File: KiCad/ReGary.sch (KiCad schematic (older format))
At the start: 10 parts, among them U4 SN74CBT16210, U5 SN74CBT16210, U6 SN74CBT16210, U7 SN74CBT16210, U8 PLCC_84_plug, U9 PLCC_84_plug

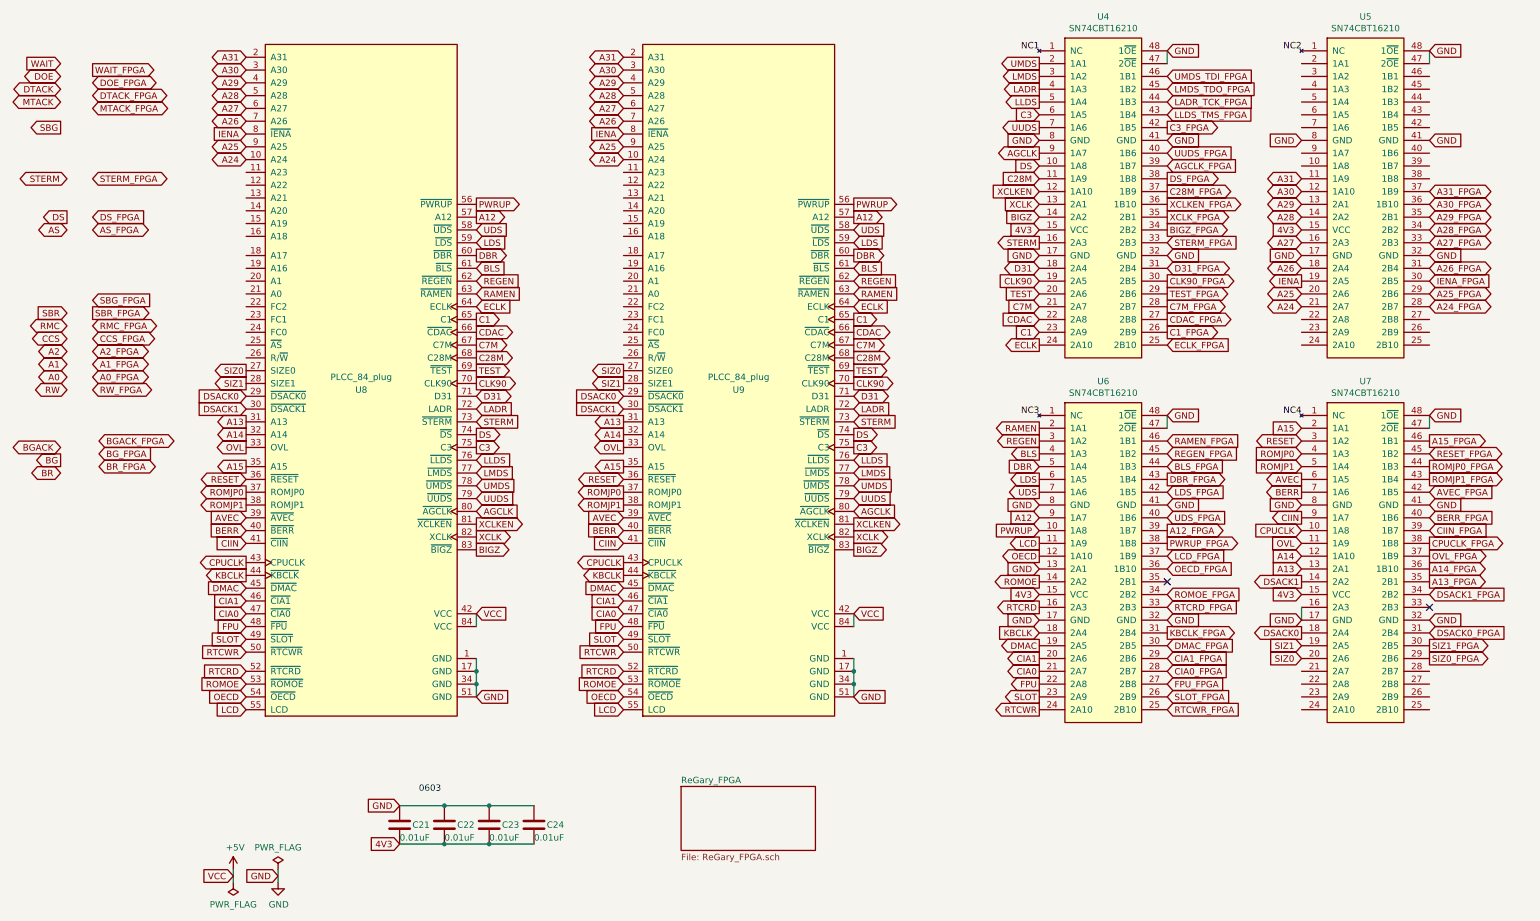
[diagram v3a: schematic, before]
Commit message: More pin assignments and routing
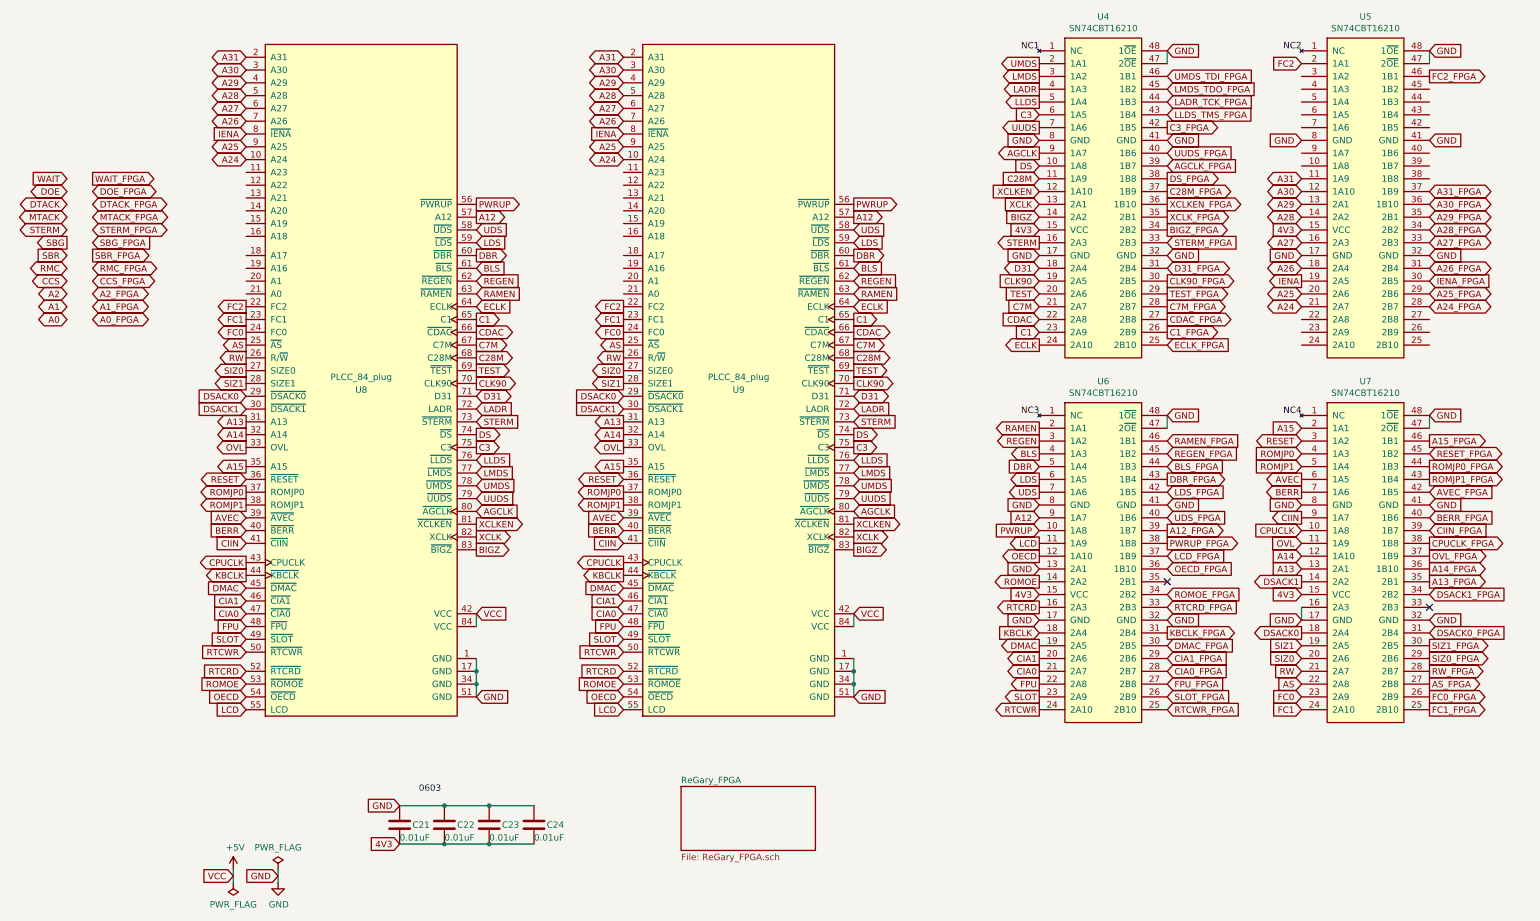
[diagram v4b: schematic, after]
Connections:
- net AS: now also U7.22 (2A8), U8.25 (~AS), U9.25 (~AS)
- net AS_FPGA: now also U7.27 (2B8)
- net RW: now also U7.21 (2A7), U8.26 (R/~W), U9.26 (R/~W)
- net RW_FPGA: now also U7.28 (2B7)
- net FC2: now reaches U5.2 (1A1)
- net FC2: now also U8.22 (FC2), U9.22 (FC2)
- net FC2_FPGA: now reaches U5.46 (1B1)
- net FC0: now reaches U7.23 (2A9)
- net FC0: now also U8.24 (FC0), U9.24 (FC0)
- net FC1: now reaches U7.24 (2A10)
- net FC1: now also U8.23 (FC1), U9.23 (FC1)
- net FC1_FPGA: now reaches U7.25 (2B10)
- net FC0_FPGA: now reaches U7.26 (2B9)
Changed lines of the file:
@@
 Text GLabel 8150 1950 2    50   Output ~ 0
 DS_FPGA
-Text GLabel -250 1100 2    50   Output ~ 0
+Text GLabel -250 1950 2    50   Output ~ 0
 WAIT_FPGA
-Text GLabel -250 1200 2    50   BiDi ~ 0
+Text GLabel -250 2050 2    50   BiDi ~ 0
 DOE_FPGA
-Text GLabel -250 1300 2    50   BiDi ~ 0
+Text GLabel -250 2150 2    50   BiDi ~ 0
 DTACK_FPGA
-Text GLabel -250 1400 2    50   BiDi ~ 0
+Text GLabel -250 2250 2    50   BiDi ~ 0
 MTACK_FPGA
-Text GLabel -250 3000 2    50   Output ~ 0
+Text GLabel -250 2550 2    50   Output ~ 0
 SBR_FPGA
-Text GLabel -250 3100 2    50   BiDi ~ 0
+Text GLabel -250 2650 2    50   BiDi ~ 0
 RMC_FPGA
-Text GLabel -250 3200 2    50   BiDi ~ 0
+Text GLabel -250 2750 2    50   BiDi ~ 0
 CCS_FPGA
-Text GLabel -250 3300 2    50   BiDi ~ 0
+Text GLabel -250 2850 2    50   BiDi ~ 0
 A2_FPGA
-Text GLabel -250 3400 2    50   BiDi ~ 0
+Text GLabel -250 2950 2    50   BiDi ~ 0
 A1_FPGA
-Text GLabel -250 2900 2    50   Input ~ 0
+Text GLabel -250 2450 2    50   Input ~ 0
 SBG_FPGA
-Text GLabel -250 3600 2    50   BiDi ~ 0
+Text GLabel 10200 5800 2    50   Output ~ 0
 RW_FPGA
 Text GLabel 10200 5700 2    50   Output ~ 0
 SIZ0_FPGA
-Text GLabel -250 1950 2    50   BiDi ~ 0
+Text GLabel -250 2350 2    50   BiDi ~ 0
 STERM_FPGA
-Text GLabel -250 2250 2    50   Input ~ 0
-DS_FPGA
-Text GLabel -250 2350 2    50   BiDi ~ 0
+Text GLabel 10200 5900 2    50   Output ~ 0
 AS_FPGA
 Text GLabel 8150 4000 2    50   Input ~ 0
@@
 Text GLabel 10200 4800 2    50   Output ~ 0
 CPUCLK_FPGA
-Text GLabel -200 4000 2    50   BiDi ~ 0
-BGACK_FPGA
-Text GLabel -200 4100 2    50   Input ~ 0
-BG_FPGA
-Text GLabel -200 4200 2    50   BiDi ~ 0
-BR_FPGA
+Text GLabel 10200 1150 2    50   Output ~ 0
+FC2_FPGA
+Text GLabel 10200 6100 2    50   Output ~ 0
+FC1_FPGA
+Text GLabel 10200 6000 2    50   Output ~ 0
+FC0_FPGA
 Wire Wire Line
 	2850 6850 3200 6850
@@
 Text GLabel 8150 2250 2    50   Output ~ 0
 XCLK_FPGA
-Text GLabel -450 3200 0    50   BiDi ~ 0
+Text GLabel -450 2750 0    50   BiDi ~ 0
 CCS
-Text GLabel -450 3300 0    50   BiDi ~ 0
+Text GLabel -450 2850 0    50   BiDi ~ 0
 A2
-Text GLabel -450 3400 0    50   BiDi ~ 0
+Text GLabel -450 2950 0    50   BiDi ~ 0
 A1
-Text GLabel -450 3500 0    50   BiDi ~ 0
+Text GLabel -450 3050 0    50   BiDi ~ 0
 A0
-Text GLabel -450 3600 0    50   BiDi ~ 0
+Text GLabel 950  3350 0    50   Output ~ 0
 RW
 Text GLabel 950  3450 0    50   Output ~ 0
@@
 Text GLabel 950  3550 0    50   Output ~ 0
 SIZ1
-Text GLabel -450 2350 0    50   BiDi ~ 0
+Text GLabel 950  3250 0    50   Output ~ 0
 AS
-Text GLabel -450 2250 0    50   Output ~ 0
-DS
 Text GLabel 950  3650 0    50   Input ~ 0
 DSACK0
 Text GLabel 950  3750 0    50   Input ~ 0
 DSACK1
-Text GLabel -450 1950 0    50   BiDi ~ 0
+Text GLabel -450 2350 0    50   BiDi ~ 0
 STERM
-Text GLabel -450 3100 0    50   BiDi ~ 0
+Text GLabel -450 2650 0    50   BiDi ~ 0
 RMC
-Text GLabel -450 3000 0    50   Input ~ 0
+Text GLabel -450 2550 0    50   Input ~ 0
 SBR
-Text GLabel -500 1550 0    50   Output ~ 0
+Text GLabel -450 2450 0    50   Output ~ 0
 SBG
-Text GLabel -500 1350 0    50   BiDi ~ 0
+Text GLabel -450 2250 0    50   BiDi ~ 0
 MTACK
-Text GLabel -500 1250 0    50   BiDi ~ 0
+Text GLabel -450 2150 0    50   BiDi ~ 0
 DTACK
-Text GLabel -500 1150 0    50   BiDi ~ 0
+Text GLabel -450 2050 0    50   BiDi ~ 0
 DOE
-Text GLabel -500 1050 0    50   Input ~ 0
+Text GLabel -450 1950 0    50   Input ~ 0
 WAIT
-Text GLabel -500 4250 0    50   BiDi ~ 0
-BR
-Text GLabel -500 4150 0    50   Output ~ 0
-BG
-Text GLabel -500 4050 0    50   BiDi ~ 0
-BGACK
+Text GLabel 950  3150 0    50   Output ~ 0
+FC0
+Text GLabel 950  3050 0    50   Output ~ 0
+FC1
+Text GLabel 950  2950 0    50   Output ~ 0
+FC2
 Text GLabel 2750 2450 2    50   Input ~ 0
 LDS
@@
 Text GLabel 8150 1550 2    50   Output ~ 0
 C3_FPGA
-Text GLabel -250 3500 2    50   BiDi ~ 0
+Text GLabel -250 3050 2    50   BiDi ~ 0
 A0_FPGA
 Text GLabel 10200 5200 2    50   Input ~ 0
@@
 Text GLabel 9200 5600 0    50   Input ~ 0
 SIZ1
+Text GLabel 3900 3350 0    50   Output ~ 0
+RW
+Text GLabel 9200 5800 0    50   Input ~ 0
+RW
+Text GLabel 3900 3250 0    50   Output ~ 0
+AS
+Text GLabel 9200 5900 0    50   Input ~ 0
+AS
+Text GLabel 3900 3150 0    50   Output ~ 0
+FC0
+Text GLabel 3900 3050 0    50   Output ~ 0
+FC1
+Text GLabel 3900 2950 0    50   Output ~ 0
+FC2
+Text GLabel 9200 6000 0    50   Input ~ 0
+FC0
+Text GLabel 9200 6100 0    50   Input ~ 0
+FC1
+Text GLabel 9200 1050 0    50   Input ~ 0
+FC2
 $EndSCHEMATC

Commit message: More signals to pin assignments and more routing done
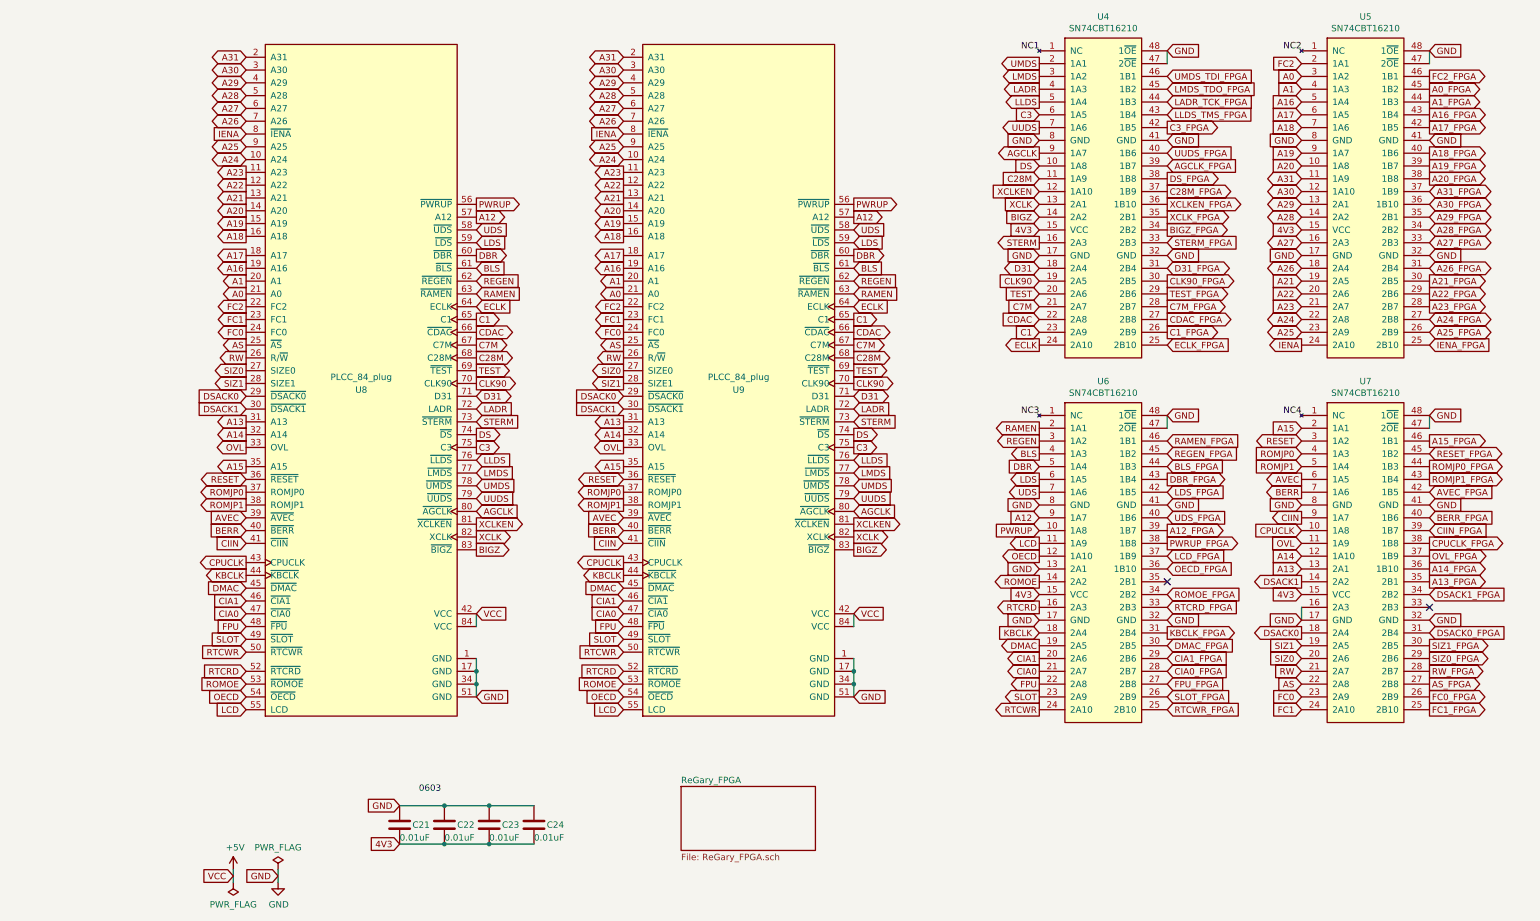
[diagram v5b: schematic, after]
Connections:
- net A0: now also U5.3 (1A2), U8.21 (A0), U9.21 (A0)
- net A0_FPGA: now also U5.45 (1B2)
- net A1: now also U5.4 (1A3), U8.20 (A1), U9.20 (A1)
- net A1_FPGA: now also U5.44 (1B3)
- net A24: now also U5.22 (2A8); no longer U5.21 (2A7)
- net A24_FPGA: now also U5.27 (2B8); no longer U5.28 (2B7)
- net A25: now also U5.23 (2A9); no longer U5.20 (2A6)
- net A25_FPGA: now also U5.26 (2B9); no longer U5.29 (2B6)
- net IENA: now also U5.24 (2A10); no longer U5.19 (2A5)
- net IENA_FPGA: now also U5.25 (2B10); no longer U5.30 (2B5)
- net A20: now reaches U5.10 (1A8)
- net A20: now also U8.14 (A20), U9.14 (A20)
- net A20_FPGA: now reaches U5.38 (1B8)
- net A19_FPGA: now reaches U5.39 (1B7)
- net A18_FPGA: now reaches U5.40 (1B6)
- net A17_FPGA: now reaches U5.42 (1B5)
- net A16_FPGA: now reaches U5.43 (1B4)
- net A16: now reaches U5.5 (1A4)
- net A16: now also U8.19 (A16), U9.19 (A16)
- net A17: now reaches U5.6 (1A5)
- net A17: now also U8.18 (A17), U9.18 (A17)
- net A18: now reaches U5.7 (1A6)
- net A18: now also U8.16 (A18), U9.16 (A18)
- net A19: now reaches U5.9 (1A7)
- net A19: now also U8.15 (A19), U9.15 (A19)
- net A23: now reaches U9.11 (A23)
- net A23: now also U5.21 (2A7), U8.11 (A23)
- net A22: now reaches U9.12 (A22)
- net A22: now also U5.20 (2A6), U8.12 (A22)
- net A21: now reaches U9.13 (A21)
- net A21: now also U5.19 (2A5), U8.13 (A21)
- new net A21_FPGA: U5.30 (2B5)
- new net A22_FPGA: U5.29 (2B6)
- new net A23_FPGA: U5.28 (2B7)
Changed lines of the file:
@@
 Text GLabel 8150 1950 2    50   Output ~ 0
 DS_FPGA
-Text GLabel -250 1950 2    50   Output ~ 0
-WAIT_FPGA
-Text GLabel -250 2050 2    50   BiDi ~ 0
-DOE_FPGA
-Text GLabel -250 2150 2    50   BiDi ~ 0
-DTACK_FPGA
-Text GLabel -250 2250 2    50   BiDi ~ 0
-MTACK_FPGA
-Text GLabel -250 2550 2    50   Output ~ 0
-SBR_FPGA
-Text GLabel -250 2650 2    50   BiDi ~ 0
-RMC_FPGA
-Text GLabel -250 2750 2    50   BiDi ~ 0
-CCS_FPGA
-Text GLabel -250 2850 2    50   BiDi ~ 0
-A2_FPGA
-Text GLabel -250 2950 2    50   BiDi ~ 0
+Text GLabel 10200 1350 2    50   Output ~ 0
 A1_FPGA
-Text GLabel -250 2450 2    50   Input ~ 0
-SBG_FPGA
 Text GLabel 10200 5800 2    50   Output ~ 0
 RW_FPGA
 Text GLabel 10200 5700 2    50   Output ~ 0
 SIZ0_FPGA
-Text GLabel -250 2350 2    50   BiDi ~ 0
-STERM_FPGA
 Text GLabel 10200 5900 2    50   Output ~ 0
 AS_FPGA
@@
 Text GLabel 8150 2250 2    50   Output ~ 0
 XCLK_FPGA
-Text GLabel -450 2750 0    50   BiDi ~ 0
-CCS
-Text GLabel -450 2850 0    50   BiDi ~ 0
-A2
-Text GLabel -450 2950 0    50   BiDi ~ 0
+Text GLabel 950  2750 0    50   Output ~ 0
 A1
-Text GLabel -450 3050 0    50   BiDi ~ 0
+Text GLabel 950  2850 0    50   Output ~ 0
 A0
 Text GLabel 950  3350 0    50   Output ~ 0
@@
 Text GLabel 950  3750 0    50   Input ~ 0
 DSACK1
-Text GLabel -450 2350 0    50   BiDi ~ 0
-STERM
-Text GLabel -450 2650 0    50   BiDi ~ 0
-RMC
-Text GLabel -450 2550 0    50   Input ~ 0
-SBR
-Text GLabel -450 2450 0    50   Output ~ 0
-SBG
-Text GLabel -450 2250 0    50   BiDi ~ 0
-MTACK
-Text GLabel -450 2150 0    50   BiDi ~ 0
-DTACK
-Text GLabel -450 2050 0    50   BiDi ~ 0
-DOE
-Text GLabel -450 1950 0    50   Input ~ 0
-WAIT
 Text GLabel 950  3150 0    50   Output ~ 0
 FC0
@@
 Text GLabel 8150 1550 2    50   Output ~ 0
 C3_FPGA
-Text GLabel -250 3050 2    50   BiDi ~ 0
+Text GLabel 10200 1250 2    50   Output ~ 0
 A0_FPGA
 Text GLabel 10200 5200 2    50   Input ~ 0
@@
 Text GLabel 9200 2650 0    50   BiDi ~ 0
 A26
-Text GLabel 9200 2750 0    50   Output ~ 0
+Text GLabel 9200 3250 0    50   Output ~ 0
 IENA
-Text GLabel 9200 2850 0    50   BiDi ~ 0
+Text GLabel 9200 3150 0    50   BiDi ~ 0
 A25
-Text GLabel 9200 2950 0    50   BiDi ~ 0
+Text GLabel 9200 3050 0    50   BiDi ~ 0
 A24
 Text GLabel 10200 2050 2    50   BiDi ~ 0
@@
 Text GLabel 10200 2650 2    50   BiDi ~ 0
 A26_FPGA
-Text GLabel 10200 2750 2    50   Input ~ 0
+Text GLabel 10200 3250 2    50   Input ~ 0
 IENA_FPGA
-Text GLabel 10200 2850 2    50   BiDi ~ 0
+Text GLabel 10200 3150 2    50   BiDi ~ 0
 A25_FPGA
-Text GLabel 10200 2950 2    50   BiDi ~ 0
+Text GLabel 10200 3050 2    50   BiDi ~ 0
 A24_FPGA
 Text GLabel 3900 3650 0    50   Input ~ 0
@@
 Text GLabel 9200 1050 0    50   Input ~ 0
 FC2
+Text GLabel 950  2650 0    50   Output ~ 0
+A16
+Text GLabel 950  2550 0    50   Output ~ 0
+A17
+Text GLabel 950  2400 0    50   Output ~ 0
+A18
+Text GLabel 950  2300 0    50   Output ~ 0
+A19
+Text GLabel 950  2200 0    50   Output ~ 0
+A20
+Text GLabel 950  2100 0    50   Output ~ 0
+A21
+Text GLabel 950  2000 0    50   Output ~ 0
+A22
+Text GLabel 950  1900 0    50   Output ~ 0
+A23
+Text GLabel 3900 2750 0    50   Output ~ 0
+A1
+Text GLabel 3900 2850 0    50   Output ~ 0
+A0
+Text GLabel 3900 2650 0    50   Output ~ 0
+A16
+Text GLabel 3900 2550 0    50   Output ~ 0
+A17
+Text GLabel 3900 2400 0    50   Output ~ 0
+A18
+Text GLabel 3900 2300 0    50   Output ~ 0
+A19
+Text GLabel 3900 2200 0    50   Output ~ 0
+A20
+Text GLabel 3900 2100 0    50   Output ~ 0
+A21
+Text GLabel 3900 2000 0    50   Output ~ 0
+A22
+Text GLabel 3900 1900 0    50   Output ~ 0
+A23
+Text GLabel 9200 1350 0    50   Input ~ 0
+A16
+Text GLabel 9200 1450 0    50   Input ~ 0
+A17
+Text GLabel 9200 1550 0    50   Input ~ 0
+A18
+Text GLabel 9200 1750 0    50   Input ~ 0
+A19
+Text GLabel 9200 1850 0    50   Input ~ 0
+A20
+Text GLabel 9200 2750 0    50   Input ~ 0
+A21
+Text GLabel 9200 2850 0    50   Input ~ 0
+A22
+Text GLabel 9200 2950 0    50   Input ~ 0
+A23
+Text GLabel 9200 1250 0    50   Input ~ 0
+A1
+Text GLabel 9200 1150 0    50   Input ~ 0
+A0
+Text GLabel 10200 1450 2    50   Output ~ 0
+A16_FPGA
+Text GLabel 10200 1550 2    50   Output ~ 0
+A17_FPGA
+Text GLabel 10200 1750 2    50   Output ~ 0
+A18_FPGA
+Text GLabel 10200 1850 2    50   Output ~ 0
+A19_FPGA
+Text GLabel 10200 1950 2    50   Output ~ 0
+A20_FPGA
+Text GLabel 10200 2750 2    50   Output ~ 0
+A21_FPGA
+Text GLabel 10200 2850 2    50   Output ~ 0
+A22_FPGA
+Text GLabel 10200 2950 2    50   Output ~ 0
+A23_FPGA
 $EndSCHEMATC

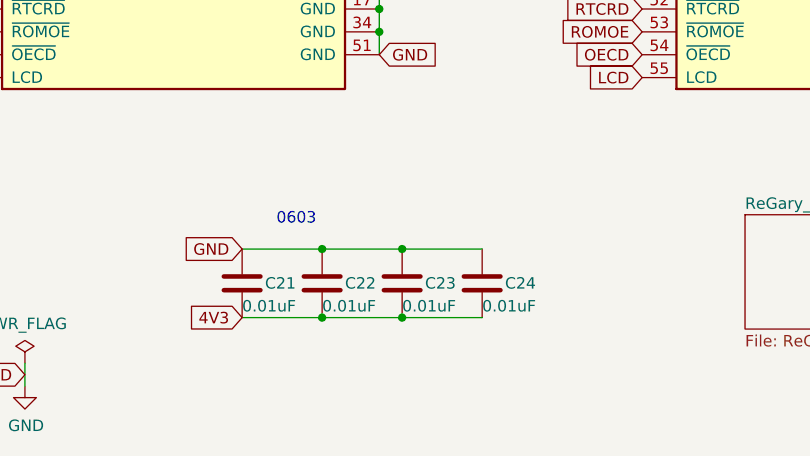
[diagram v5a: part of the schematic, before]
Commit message: Fixed enumeration of capacitors and placement of last capacitor C11 for 3V3-power
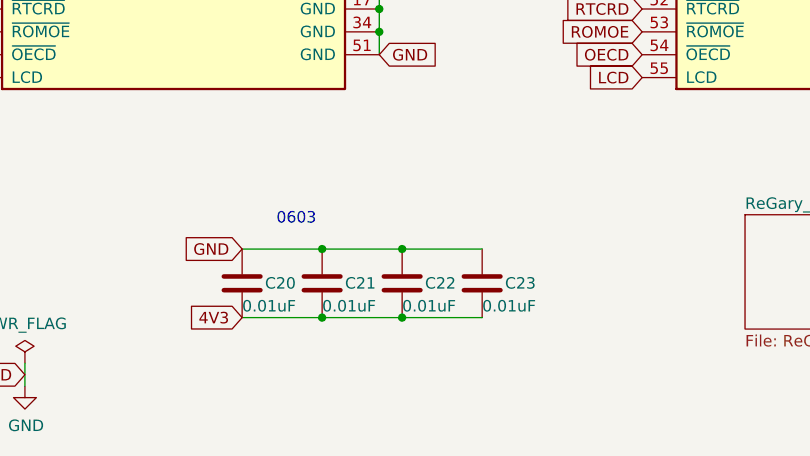
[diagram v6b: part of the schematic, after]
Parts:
- renumbered C21 to C20, C22 to C21, C23 to C22, C24 to C23
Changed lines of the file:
@@
 0603
 $Comp
-L Device:C C24
+L Device:C C23
 U 1 1 605F0F7B
 P 3200 7000
-F 0 "C24" H 3300 7000 50  0000 L CNN
+F 0 "C23" H 3300 7000 50  0000 L CNN
 F 1 "0.01uF" H 3200 6900 50  0000 L CNN
 F 2 "Capacitor_SMD:C_0603_1608Metric_Pad1.05x0.95mm_HandSolder" H 3238 6850 50  0001 C CNN
@@
 $EndComp
 $Comp
-L Device:C C23
+L Device:C C22
 U 1 1 605D5D6F
 P 2850 7000
-F 0 "C23" H 2950 7000 50  0000 L CNN
+F 0 "C22" H 2950 7000 50  0000 L CNN
 F 1 "0.01uF" H 2850 6900 50  0000 L CNN
 F 2 "Capacitor_SMD:C_0603_1608Metric_Pad1.05x0.95mm_HandSolder" H 2888 6850 50  0001 C CNN
@@
 $EndComp
 $Comp
-L Device:C C22
+L Device:C C21
 U 1 1 605D5659
 P 2500 7000
-F 0 "C22" H 2600 7000 50  0000 L CNN
+F 0 "C21" H 2600 7000 50  0000 L CNN
 F 1 "0.01uF" H 2500 6900 50  0000 L CNN
 F 2 "Capacitor_SMD:C_0603_1608Metric_Pad1.05x0.95mm_HandSolder" H 2538 6850 50  0001 C CNN
@@
 $EndComp
 $Comp
-L Device:C C21
+L Device:C C20
 U 1 1 605D3E60
 P 2150 7000
-F 0 "C21" H 2250 7000 50  0000 L CNN
+F 0 "C20" H 2250 7000 50  0000 L CNN
 F 1 "0.01uF" H 2150 6900 50  0000 L CNN
 F 2 "Capacitor_SMD:C_0603_1608Metric_Pad1.05x0.95mm_HandSolder" H 2188 6850 50  0001 C CNN
